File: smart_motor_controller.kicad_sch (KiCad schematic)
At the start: 38 parts, among them J10 USB_B_Micro, J101 Conn_02x07_Odd_Even, J102 I2C_CONN, J104 Debug, J9 Input 12V, SW102 SW_NRST, SW103 SW_NRST, U2 STM32F405RGT6, U3 USBLC6-2SC6

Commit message: Initial changes
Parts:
- removed J10: USB_B_Micro, VsReality_Footprints:U-F-M5DD-W-L, symbol Connector:USB_B_Micro
- removed J104: Debug, Connector_PinHeader_2.54mm:PinHeader_1x04_P2.54mm_Vertical, symbol smart_motor_controller-rescue:Conn_01x04_Male-Connector
- removed R103, R104: 15, Resistor_SMD:R_0603_1608Metric, symbol Device:R_Small
- removed TP2: 5V, TestPoint:TestPoint_Pad_D2.0mm, symbol Connector:TestPoint_Small
- removed U2: STM32F405RGT6, Package_QFP:LQFP-64_10x10mm_P0.5mm, symbol smart_motor_controller-rescue:STM32F405RGTx-MCU_ST_STM32F4
- removed U3: USBLC6-2SC6, Package_TO_SOT_SMD:SOT-23-6, symbol Power_Protection:USBLC6-2SC6
- added C1, C2, C9: 100nf, Capacitor_SMD:C_0603_1608Metric, symbol Device:C_Small
- added J104: SWD, Connector_PinHeader_1.27mm:PinHeader_2x05_P1.27mm_Vertical, symbol Connector_Generic:Conn_02x05_Odd_Even
- added U1: STM32F405VGTx, Package_QFP:LQFP-100_14x14mm_P0.5mm, symbol MCU_ST_STM32F4:STM32F405VGTx
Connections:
- net +3.3VA: now also U1.22 (VDDA)
- net +3V3: now also C1.1, C2.1, C9.1, J104.1 (Pin_1), U1.100 (VDD), U1.11 (VDD), U1.19 (VDD), U1.21 (VREF+), U1.28 (VDD), U1.50 (VDD), U1.6 (VBAT), U1.75 (VDD)
- net BOOT0: now also U1.94 (BOOT0)
- net CAN2_RX: now also U1.51 (PB12)
- net CAN2_TX: now also U1.52 (PB13)
- net ENCODER_0_A: now also U1.31 (PA6)
- net ENCODER_0_B: now also U1.32 (PA7)
- net ENCODER_1_A: now also U1.23 (PA0)
- net ENCODER_1_B: now also U1.24 (PA1)
- net ENCODER_2_A: now also U1.92 (PB6)
- net ENCODER_2_B: now also U1.93 (PB7)
- net ENCODER_3_A: now also U1.77 (PA15)
- net ENCODER_3_B: now also U1.89 (PB3)
- net GND: now also C1.2, C2.2, C9.2, J104.3 (Pin_3), J104.5 (Pin_5), J104.9 (Pin_9), U1.10 (VSS), U1.20 (VSSA), U1.27 (VSS), U1.74 (VSS), U1.99 (VSS)
- net GPIO0: now also U1.91 (PB5)
- net GPIO1: now also U1.90 (PB4)
- net GPIO2: now also U1.83 (PD2)
- net GPIO3: now also U1.80 (PC12)
- net HSE_IN: now also U1.12 (PH0)
- net HSE_OUT: now also U1.13 (PH1)
- net I2C1_SCL: now also U1.95 (PB8)
- net I2C1_SDA: now also U1.96 (PB9)
- net I2C2_SCL: now also U1.47 (PB10)
- net I2C2_SDA: now also U1.48 (PB11)
- net LED: now also U1.25 (PA2)
- net NRST: now also J104.10 (Pin_10), U1.14 (NRST)
- net SWCLK: now also J104.4 (Pin_4), U1.76 (PA14)
- net SWDIO: now also J104.2 (Pin_2), U1.72 (PA13)
- net USART3_RX: now also U1.79 (PC11)
- net USART3_TX: now also U1.78 (PC10)
- net USB_D+: now also U1.71 (PA12)
- net USB_D-: now also U1.70 (PA11)
- net at C15.1: now also U1.49 (VCAP_1)
- net at C16.1: now also U1.73 (VCAP_2)
- new net M0_EN: U1.63 (PC6)
- new net M1_EN: U1.64 (PC7)
- new net M2_EN: U1.65 (PC8)
- new net M3_EN: U1.66 (PC9)
- new net SWO: J104.6 (Pin_6)
- no-connect marks 18 -> 49
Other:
- added sheet Encoders (encoders.kicad_sch)
- added sheet IMU (IMU.kicad_sch)
- added sheet USB (usb.kicad_sch)
- note removed: "App note: AN4879"
- moved on the sheet: C101, C13, C14, C15, C16, C17, C18, C3, C4, C5, C6, C7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

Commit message: Add USB sensing and power management components to the schematic
- Introduced a junction for USB sensing at coordinates (173.99, 64.77).
- Added multiple wires connecting various components to the new junction.
- Created a global label "USB_SENSE" for the USB sensing functionality.
- Updated references for power components to a new numbering scheme (#PWR0501 to #PWR0509).
- Added resistors R505 and R506 with specified values and footprints.
- Included power symbols for +5V and GND with appropriate references and properties.
- Ensured all new components are included in the BOM and marked for simulation.
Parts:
- renumbered C13 to C101, C14 to C102, C101 to C103, C17 to C104, C18 to C105, C3 to C106, C4 to C107, C5 to C108, C6 to C109, C7 to C110, C8 to C111, C1 to C112, C2 to C113, C9 to C114, C15 to C115, C16 to C116, D1 to D101, D2 to D102, D101 to D103, D3 to D104, HSE1 to HSE101, J102 to J101, J104 to J102, J9 to J103, J101 to J104, L2 to L101, R14 to R101, R15 to R102, R102 to R103, R101 to R104, R6 to R105, R7 to R106, SW103 to SW101, TP1 to TP101, U1 to U101
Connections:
- net CAN2_RX: no longer U101.51 (PB12)
- net CAN2_TX: no longer U101.52 (PB13)
- net ENCODER_3_A: now also U101.63 (PC6); no longer U101.77 (PA15)
- net ENCODER_3_B: now also U101.64 (PC7); no longer U101.89 (PB3)
- net GPIO0: no longer U101.91 (PB5)
- net GPIO1: no longer U101.90 (PB4)
- net GPIO2: no longer U101.83 (PD2)
- net GPIO3: no longer U101.80 (PC12)
- net I2C1_SCL: no longer U101.95 (PB8)
- net I2C1_SDA: no longer U101.96 (PB9)
- net I2C2_SCL: no longer U101.47 (PB10)
- net I2C2_SDA: no longer U101.48 (PB11)
- net M0_EN: now also U101.39 (PE8); no longer U101.63 (PC6)
- net M1_EN: now also U101.41 (PE10); no longer U101.64 (PC7)
- net M2_EN: now also U101.43 (PE12); no longer U101.65 (PC8)
- net M3_EN: now also U101.46 (PE15); no longer U101.66 (PC9)
- net SWO: now also U101.89 (PB3)
- net USART3_RX: no longer U101.79 (PC11)
- net USART3_TX: no longer U101.78 (PC10)
- net IMU_MISO: now reaches U101.17 (PC2)
- net IMU_SDI: now reaches U101.18 (PC3)
- net SENSOR_SCL: now reaches U101.67 (PA8)
- net USB_SENSE: now reaches U101.68 (PA9)
- new net IMU_SCK: U101.47 (PB10)
- new net M_SCLK: U101.78 (PC10)
- new net M_SDI: U101.79 (PC11)
- new net M_SDO: U101.80 (PC12)
- new net SENSOR_SDA: U101.66 (PC9)
- no-connect marks 49 -> 43
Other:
- sheet IMU renamed Sensors
- note added: "MISO"
- note added: "MOSI"

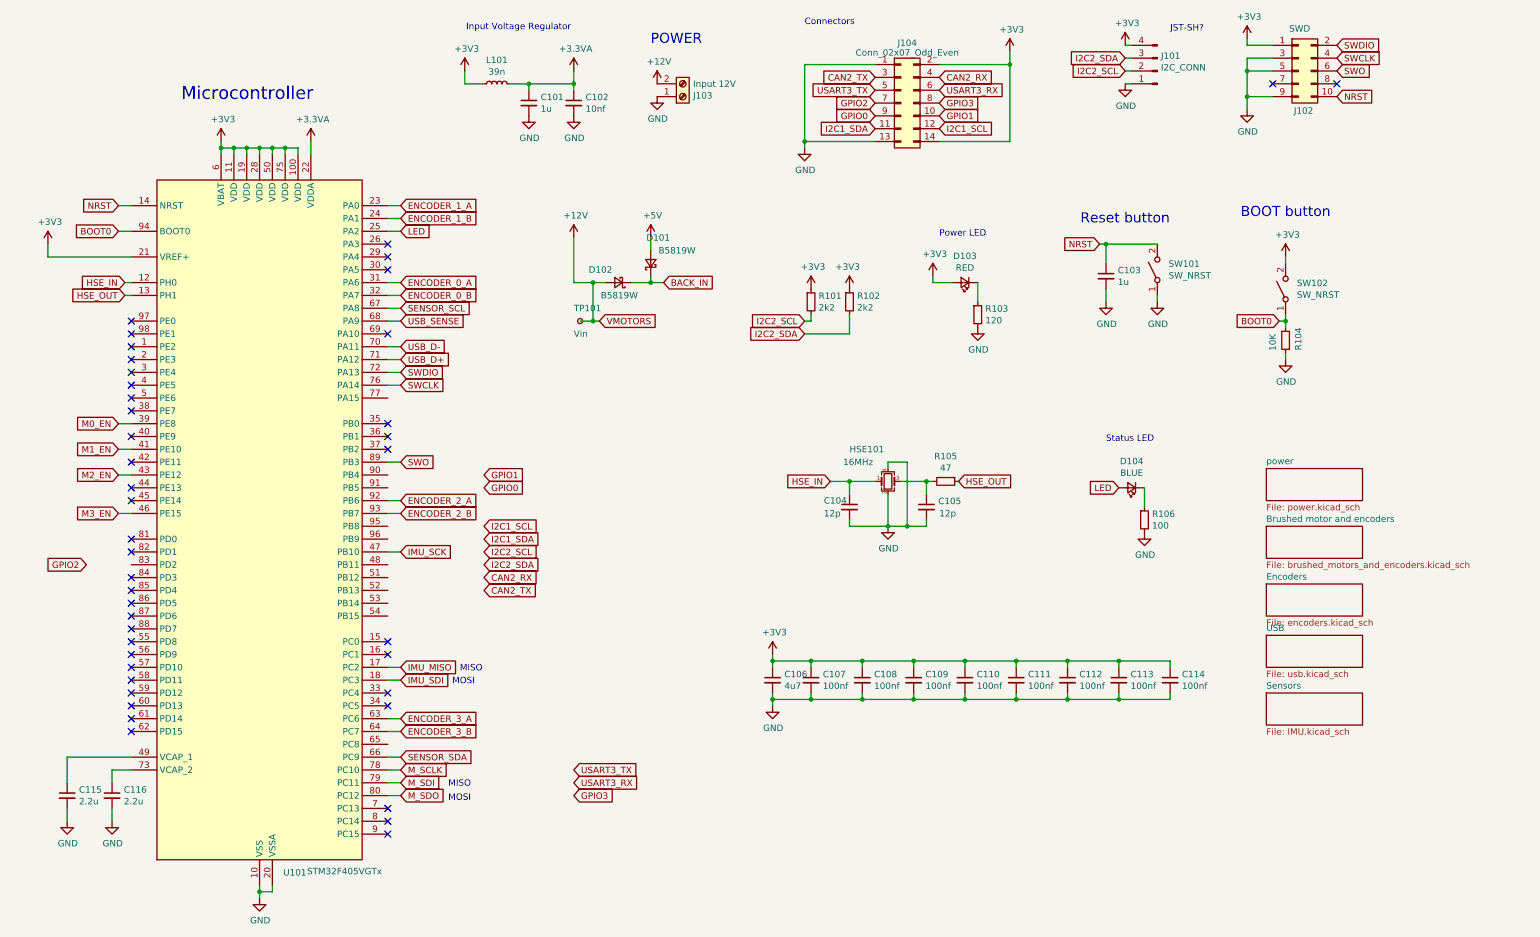
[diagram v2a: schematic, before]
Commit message: Implement structure for code changes tracking
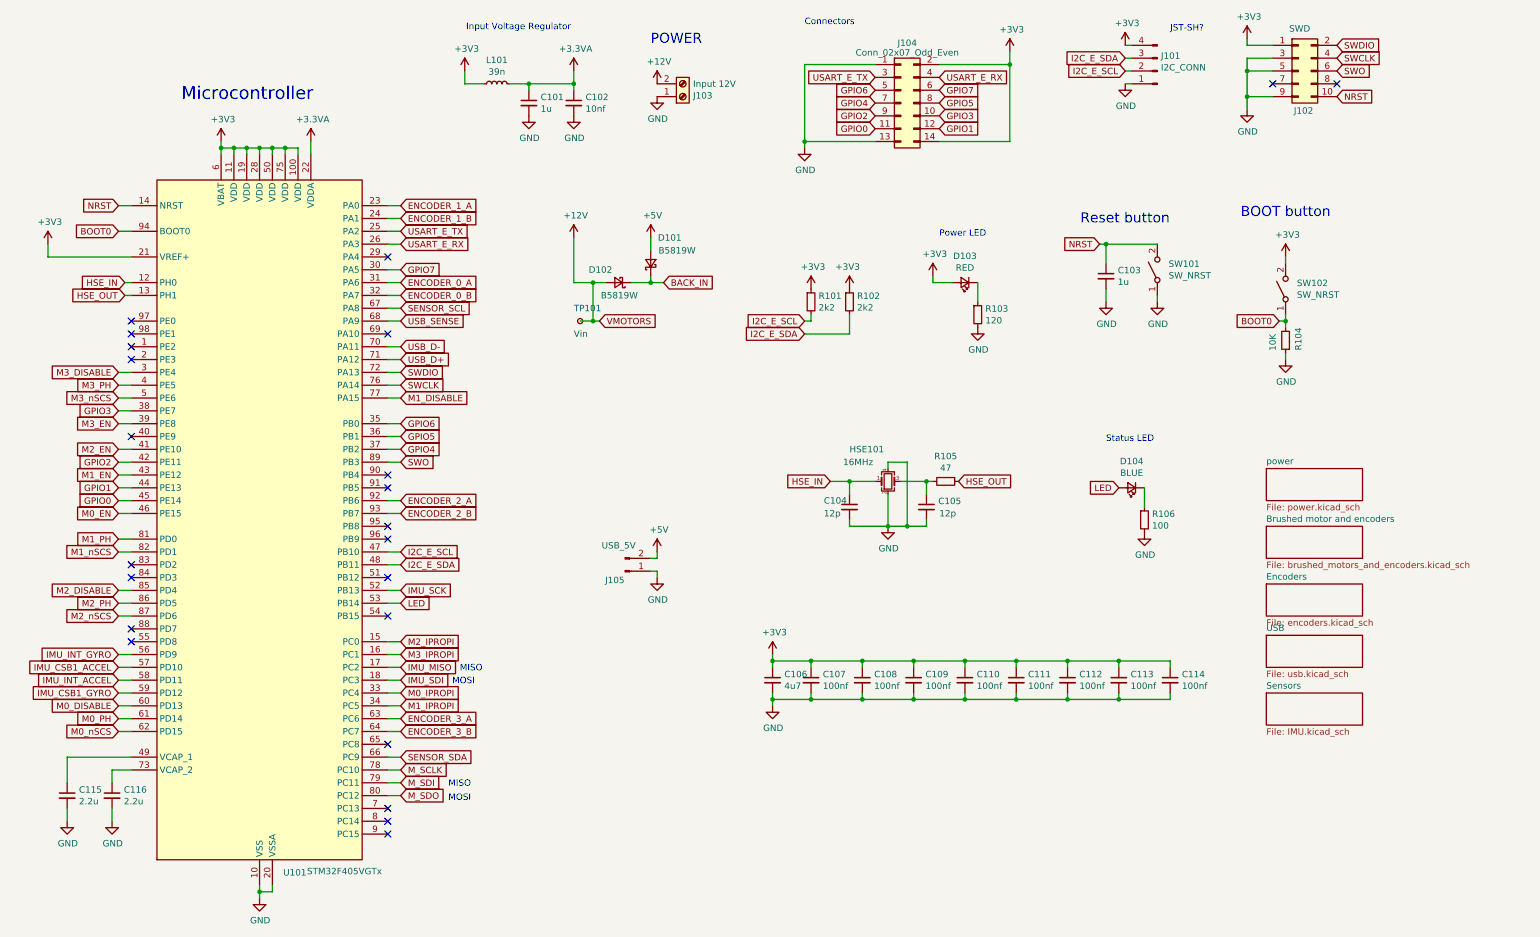
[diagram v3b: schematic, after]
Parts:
- added J105: USB_5V, Connector_PinHeader_2.54mm:PinHeader_2x01_P2.54mm_Vertical, symbol Connector:Conn_01x02_Pin
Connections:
- net CAN2_RX is gone; now on net USART_E_RX: J104.4 (Pin_4)
- net I2C1_SCL is gone; now on net GPIO1: J104.12 (Pin_12)
- net I2C1_SDA is gone; now on net GPIO0: J104.11 (Pin_11)
- net I2C2_SDA is gone; now on net I2C_E_SDA: J101.3 (Pin_3), R102.2
- net USART3_RX is gone; now on net GPIO7: J104.6 (Pin_6)
- net USART3_TX is gone; now on net GPIO6: J104.5 (Pin_5)
- net +5V: now also J105.2 (Pin_2)
- net GND: now also J105.1 (Pin_1)
- net GPIO0: now also U101.45 (PE14); no longer J104.9 (Pin_9)
- net GPIO1: now also U101.44 (PE13); no longer J104.10 (Pin_10)
- net GPIO2: now also J104.9 (Pin_9), U101.42 (PE11); no longer J104.7 (Pin_7)
- net GPIO3: now also J104.10 (Pin_10), U101.38 (PE7); no longer J104.8 (Pin_8)
- net IMU_SCK: now also U101.52 (PB13); no longer U101.47 (PB10)
- net LED: now also U101.53 (PB14); no longer U101.25 (PA2)
- net M0_EN: now also U101.46 (PE15); no longer U101.39 (PE8)
- net M1_EN: now also U101.43 (PE12); no longer U101.41 (PE10)
- net M2_EN: now also U101.41 (PE10); no longer U101.43 (PE12)
- net M3_EN: now also U101.39 (PE8); no longer U101.46 (PE15)
- net M2_IPROPI: now reaches U101.15 (PC0)
- net M3_IPROPI: now reaches U101.16 (PC1)
- net USART_E_RX: now reaches U101.26 (PA3)
- net M3_DISABLE: now reaches U101.3 (PE4)
- net GPIO7: now reaches U101.30 (PA5)
- net M0_IPROPI: now reaches U101.33 (PC4)
- net M1_IPROPI: now reaches U101.34 (PC5)
- net GPIO6: now reaches U101.35 (PB0)
- net GPIO5: now reaches U101.36 (PB1)
- net GPIO5: now also J104.8 (Pin_8)
- net GPIO4: now reaches U101.37 (PB2)
- net GPIO4: now also J104.7 (Pin_7)
- net M3_PH: now reaches U101.4 (PE5)
- net I2C_E_SDA: now reaches U101.48 (PB11)
- net M3_nSCS: now reaches U101.5 (PE6)
- net IMU_INT_GYRO: now reaches U101.56 (PD9)
- net IMU_CSB1_ACCEL: now reaches U101.57 (PD10)
- net IMU_INT_ACCEL: now reaches U101.58 (PD11)
- net IMU_CSB1_GYRO: now reaches U101.59 (PD12)
- net M0_DISABLE: now reaches U101.60 (PD13)
- net M0_PH: now reaches U101.61 (PD14)
- net M0_nSCS: now reaches U101.62 (PD15)
- net M1_DISABLE: now reaches U101.77 (PA15)
- net M1_PH: now reaches U101.81 (PD0)
- net M1_nSCS: now reaches U101.82 (PD1)
- net M2_DISABLE: now reaches U101.85 (PD4)
- net M2_PH: now reaches U101.86 (PD5)
- net M2_nSCS: now reaches U101.87 (PD6)
- net CAN2_TX renamed USART_E_TX
- net USART_E_TX: now also U101.25 (PA2)
- net I2C2_SCL renamed I2C_E_SCL
- net I2C_E_SCL: now also U101.47 (PB10)
- no-connect marks 43 -> 23
